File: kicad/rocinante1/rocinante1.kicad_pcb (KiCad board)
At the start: 2 copper layers, 138.6 x 89.2 mm, 132 parts, among them J1 ESP_01, J10 KEYBOARD, J11 SERIAL, J12 SD_Card, J13 USBFS/POWER, J14 I2S, J15 NEOPIXEL, J16 EXPHDR, J2 SWD, J3 COMPOSITE, J4 CTRL1, J5 CTRL2, J6 VGA, J7 AUDIOIN, J8 AUDIOOUT, J9 MOUSE, Q1 Q_NPN_CBE, SW1 RESET, SW2 USER1, SW3 USER2, SW4 USER3, SW5 BOOT0, U1 STM32H743IITx, U2 W9812G6KH-6, U3 LD1117S33TR_SOT223, X1 ASE-14.31818MHz, Y1 25MHz

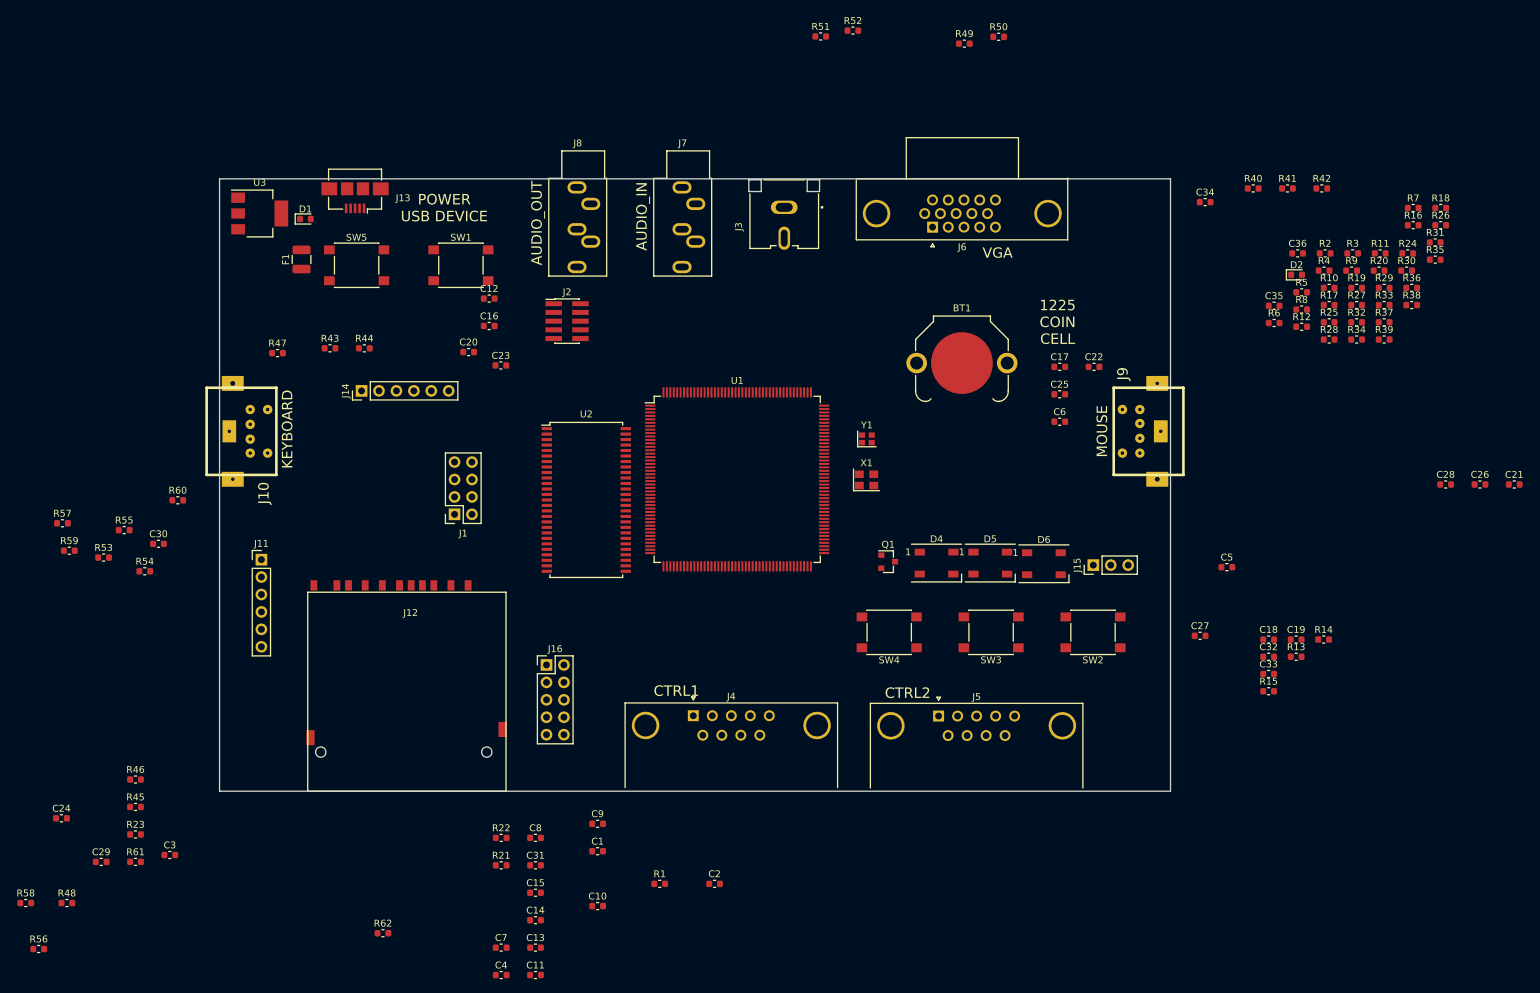
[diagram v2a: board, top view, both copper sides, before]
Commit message: Schematic done, THT PN chosen, working on routing
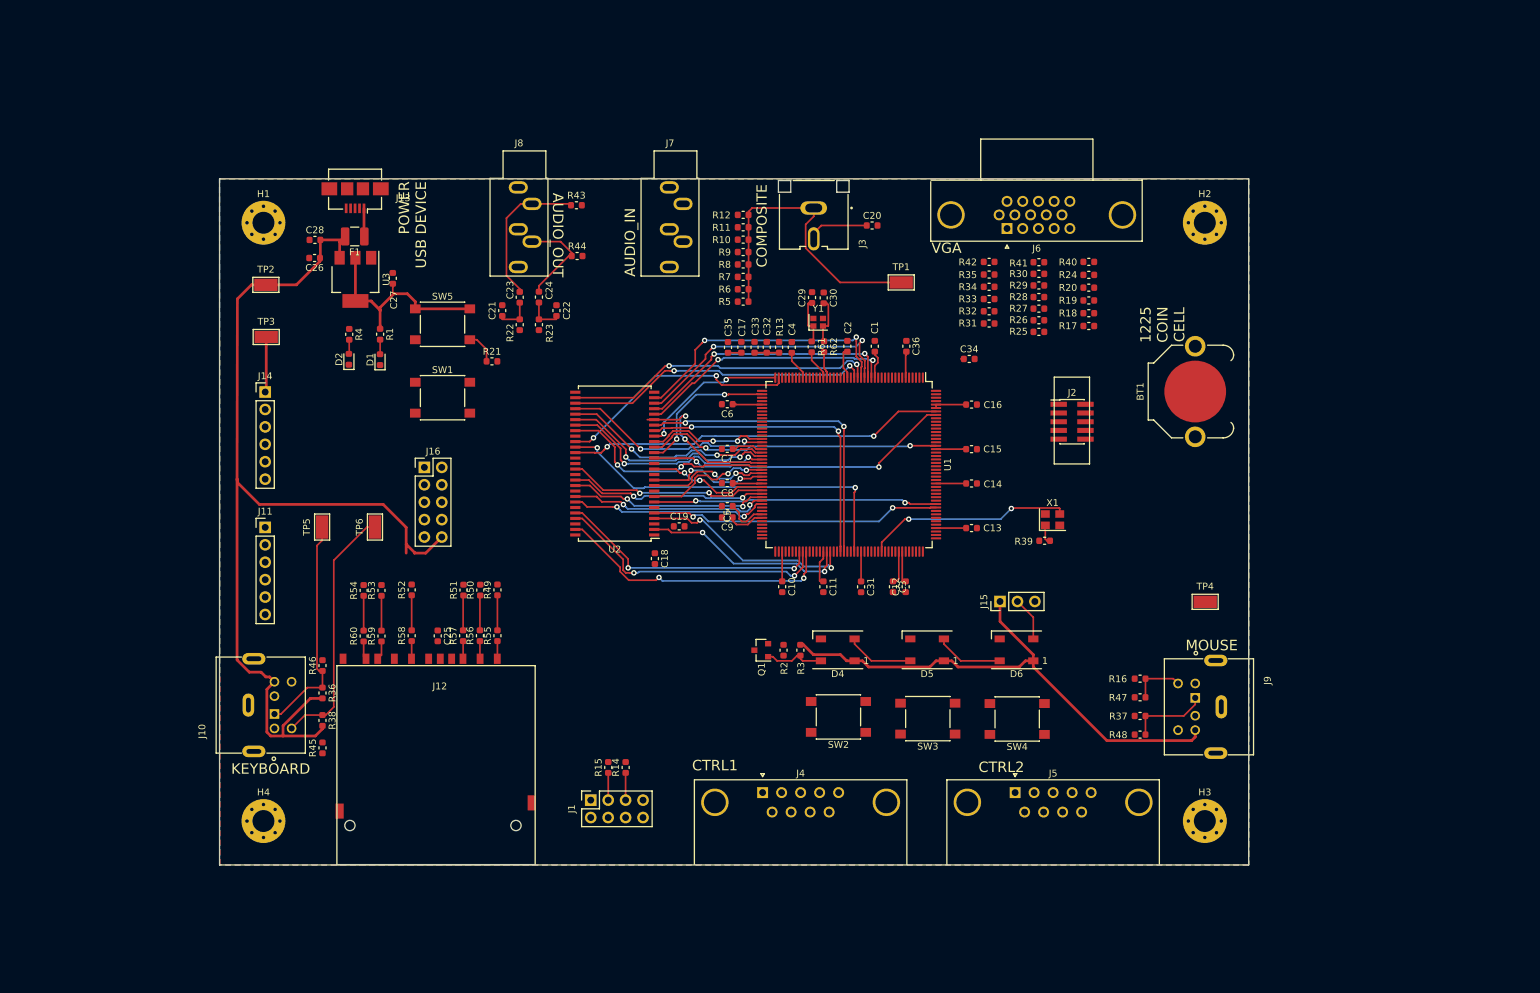
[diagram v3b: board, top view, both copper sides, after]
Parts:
- added H1: HOLE0, MountingHole:MountingHole_3.2mm_M3_Pad_Via, F.Cu at (82.0, 67.0)
- added H2: HOLE1, MountingHole:MountingHole_3.2mm_M3_Pad_Via, F.Cu at (219.2, 67.0)
- added H3: HOLE2, MountingHole:MountingHole_3.2mm_M3_Pad_Via, F.Cu at (219.2, 154.2)
- added H4: HOLE3, MountingHole:MountingHole_3.2mm_M3_Pad_Via, F.Cu at (82.0, 154.2)
- added TP1: CPST, TestPoint:TestPoint_Keystone_5015_Micro-Minature, F.Cu at (174.9, 75.7)
- added TP2: 5V, TestPoint:TestPoint_Keystone_5015_Micro-Minature, F.Cu at (82.3, 76.0)
- added TP3: 3V3, TestPoint:TestPoint_Keystone_5015_Micro-Minature, F.Cu at (82.3, 83.7)
- added TP4: GND, TestPoint:TestPoint_Keystone_5015_Micro-Minature, F.Cu at (219.2, 122.2)
- added TP5: KBDDATA, TestPoint:TestPoint_Keystone_5015_Micro-Minature, F.Cu at (90.5, 111.3)
- added TP6: KBDCLK, TestPoint:TestPoint_Keystone_5015_Micro-Minature, F.Cu at (98.2, 111.3)
- J10, J9: footprint Mini_din6:Mini_din6 -> Mini_din6:CUI_MD-60SM
- moved C26 173.0 mm to (89.4, 72.1), turned to 180 degrees
- moved R38 169.9 mm to (90.5, 139.5), turned to 270 degrees
- moved R36 169.4 mm to (90.5, 135.5), turned to 270 degrees
- moved C28 168.6 mm to (89.5, 69.5)
- moved R48 158.3 mm to (209.7, 141.6), turned to 180 degrees
- moved C21 149.7 mm to (116.8, 79.8), turned to 270 degrees
- moved R4 142.4 mm to (94.5, 83.3), turned to 270 degrees
- moved D2 138.7 mm to (94.4, 86.9), turned to 90 degrees
- moved R47 135.4 mm to (209.7, 136.2), turned to 180 degrees
- moved C29 132.3 mm to (161.9, 77.9), turned to 270 degrees
- moved C27 128.7 mm to (100.8, 75.1), turned to 90 degrees
- moved R61 123.9 mm to (161.8, 85.1), turned to 270 degrees
- moved C3 112.4 mm to (173.7, 120.0), turned to 270 degrees
- moved R50 110.5 mm to (113.5, 120.5), turned to 90 degrees
- moved R62 107.0 mm to (163.7, 85.1), turned to 270 degrees
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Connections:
- net AUDIO_IN_L renamed AUDIO_OUT_L
- net AUDIO_IN_R renamed AUDIO_OUT_R
- R14 pad 1: VDD -> ESP_GPIO0
- R14 pad 2: ESP_GPIO0 -> VDD
- R15 pad 1: VDD -> ESP_GPIO2
- R15 pad 2: ESP_GPIO2 -> VDD
- R16 pad 1: MOUSE_DATA -> MOUSE_CLK
- R37 pad 1: MOUSE_CLK -> MOUSE_DATA
- R61 pad 2: CLOCK0 -> CLOCK1
- R62 pad 2: CLOCK1 -> CLOCK0
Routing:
- net +5V: track 0.00 -> 225.5 mm
- net VDD: track 0.00 -> 112.2 mm
- net SDRAM_NBL1: track 0.00 -> 55.1 mm, vias 0 -> 2
- net SDRAM_SDCLK: track 0.00 -> 53.1 mm, vias 0 -> 2
- net SDRAM_BA1: track 0.00 -> 47.2 mm, vias 0 -> 2
- net SDRAM_A4: track 0.00 -> 45.7 mm, vias 0 -> 2
- net SDRAM_NBL0: track 0.00 -> 45.3 mm, vias 0 -> 2
- net Net-(J3-Pad1): track 0.00 -> 45.2 mm
- net SDRAM_BA0: track 0.00 -> 45.1 mm, vias 0 -> 2
- net SDRAM_A5: track 0.00 -> 44.7 mm, vias 0 -> 2
- net SDRAM_SDNCAS: track 0.00 -> 43.9 mm, vias 0 -> 2
- net SDRAM_D2: track 0.00 -> 42.7 mm, vias 0 -> 2
- net SDRAM_D3: track 0.00 -> 41.5 mm, vias 0 -> 2
- net SDRAM_D15: track 0.00 -> 41.3 mm, vias 0 -> 2
- net SDRAM_A3: track 0.00 -> 40.6 mm, vias 0 -> 2
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- added copper zone on B.Cu, net GND
- added copper zone on F.Cu, net GND
- added copper zone on In1.Cu, net GND
- added copper zone on In2.Cu, net VDD
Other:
- board size 138.6 x 89.2 mm -> 150 x 100 mm
- copper layers 2 -> 4
- net class 5V added: clearance 0.2, trace_width 0.4, via_dia 0.9, via_drill 0.5
- net class Power added: clearance 0.2, trace_width 0.25, via_dia 0.8, via_drill 0.4
- board text added: "COMPOSITE"
- board text added: "KEYBOARD"
- board text added: "MOUSE"

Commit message: add first revision of PCB
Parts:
- moved J3 27.8 mm to (142.2, 45.5)
- moved C6 27.4 mm to (130.4, 73.8), turned to 90 degrees
- moved C32 26.4 mm to (135.3, 67.8)
- moved C33 26.4 mm to (133.6, 67.8)
- moved SW3 26.4 mm to (158.8, 122.0)
- moved C29 26.4 mm to (141.9, 60.6)
- moved R10 26.4 mm to (131.9, 52.2)
- moved R11 26.4 mm to (131.9, 50.4)
- moved R32 26.4 mm to (167.8, 62.6)
- moved R33 26.4 mm to (167.8, 60.8)
- moved R42 26.4 mm to (167.8, 55.4)
- moved R6 26.4 mm to (131.9, 59.4)
- moved R7 26.4 mm to (131.9, 57.6)
- moved R8 26.4 mm to (131.9, 55.8)
- moved R9 26.4 mm to (131.9, 54.0)
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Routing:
- net +5V: track 225.5 -> 528.5 mm, vias 0 -> 7
- net GND: track 4.82 -> 177.7 mm, vias 0 -> 30
- net NRST: track 0.00 -> 131.6 mm, vias 0 -> 5
- net USB_FS_D_P: track 0.00 -> 131.1 mm, vias 0 -> 2
- net USB_FS_D_N: track 0.00 -> 130.5 mm, vias 0 -> 2
- net USART1_RX: track 0.00 -> 129.7 mm, vias 0 -> 4
- net CV0: track 0.00 -> 126.1 mm, vias 0 -> 2
- net TIM2_CH1: track 0.00 -> 125.6 mm, vias 0 -> 4
- net CV1: track 0.00 -> 123.3 mm, vias 0 -> 2
- net CV2: track 0.00 -> 115.7 mm, vias 0 -> 2
- net TIM5_CH2: track 0.00 -> 113.8 mm, vias 0 -> 2
- net ADC3_INP6: track 0.00 -> 113.2 mm, vias 0 -> 2
- net USER1: track 0.00 -> 113.2 mm, vias 0 -> 2
- net ESP_TX: track 0.00 -> 112.4 mm, vias 0 -> 2
- net JOYSELECT: track 0.00 -> 112.2 mm, vias 0 -> 2
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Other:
- net class Default: clearance 0.2 -> 0.127
- net class Power: clearance 0.2 -> 0.127
- rule trace_clearance: 0.2 -> 0.127

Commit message: add some necessary BOM fields
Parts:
- C29, C30: value TBD -> 5.1pF
- R61, R62: value TBD -> 0
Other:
- board text added: "+3.3V"
- board text added: "+5V"
- board text added: "BOOT0"
- board text added: "CK"
- board text added: "CPST"
- board text added: "CTS"
- board text added: "DEBUG"
- board text added: "DOUT"
- board text added: "ESP-01"
- board text added: "EXPHDR"
- board text added: "FTDI"
- board text added: "GND"
- board text added: "GPIO0"
- board text added: "GPIO1"
- board text added: "I2S"
- board text added: "KBDCLK"
- board text added: "KBDDATA"
- board text added: "MISO"
- board text added: "MOSI"
- board text added: "NSS"
- board text added: "POWER"
- board text added: "PWM"
- board text added: "RESET"
- board text added: "RGB1"
- board text added: "RGB2"
- board text added: "RGB3"
- board text added: "RX"
- board text added: "Rocinante V1 Sep 2020 plunk.org/rosa Brad Grantham b@plunk.org"
- board text added: "SCK"
- board text added: "SDI"
- board text added: "SDO"
- board text added: "SWD"
- board text added: "TX"
- board text added: "USER1"
- board text added: "USER2"
- board text added: "USER3"
- board text added: "VDD"
- board text added: "WS"

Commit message: make v1 PCB
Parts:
- Q1: footprint Package_TO_SOT_SMD:SOT-23 -> Package_TO_SOT_SMD:SOT-323_SC-70
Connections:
- J3 pad 1: Net-(J3-Pad1) -> Net-(C20-Pad1)
- J3 pad 2: Net-(C20-Pad1) -> Net-(J3-Pad2)
- R10 pad 1: Net-(J3-Pad1) -> Net-(J3-Pad2)
- R11 pad 1: Net-(J3-Pad1) -> Net-(J3-Pad2)
- R12 pad 1: Net-(J3-Pad1) -> Net-(J3-Pad2)
- R5 pad 1: Net-(J3-Pad1) -> Net-(J3-Pad2)
- R6 pad 1: Net-(J3-Pad1) -> Net-(J3-Pad2)
- R7 pad 1: Net-(J3-Pad1) -> Net-(J3-Pad2)
- R8 pad 1: Net-(J3-Pad1) -> Net-(J3-Pad2)
- R9 pad 1: Net-(J3-Pad1) -> Net-(J3-Pad2)
- TP1 pad 1: Net-(J3-Pad1) -> Net-(J3-Pad2)
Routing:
- net Net-(J3-Pad1): track 49.0 -> 0.00 mm
- net Net-(J3-Pad2): track 0.00 -> 39.9 mm
- net Net-(C20-Pad1): track 7.77 -> 9.91 mm
